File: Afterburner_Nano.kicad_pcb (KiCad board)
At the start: 4 copper layers, 37.9 x 36.5 mm, 86 parts, among them IC1 TPS25730DREFR, IC2 TVS3301DRBR, IC3 MCP1416T-E_OT, IC4 ADS1220IRVAR, IC5 MAX31865ATP+T, IC6 TVS3301DRBR, IC7 INA260AIPWR, IC8 AP7361E-33FGE-7, J1 USB4730-GF-A-KIT, J2 NTMFS5C612NLT1G, J3 Conn_01x04_Pin, J4 Conn_01x02_Pin, J5 USB4730-GF-A-KIT, J6 Conn_01x04_Pin, U1 TPS62933DRLR, U4 ESP32-C6-MINI-1

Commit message: layout changes
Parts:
- removed C6, C7: 330pF, Capacitor_SMD:C_0201_0603Metric
- added R29: 22, Resistor_SMD:R_0201_0603Metric, F.Cu at (197.3, 41.5)
- added R30: 22, Resistor_SMD:R_0201_0603Metric, F.Cu at (197.3, 40.7)
- added R31: 3k3, Resistor_SMD:R_0201_0603Metric, F.Cu at (188.1, 41.6)
- C14, C15: footprint Capacitor_SMD:C_0402_1005Metric -> Capacitor_SMD:C_0805_2012Metric
- C18: footprint Capacitor_SMD:C_0201_0603Metric -> Capacitor_SMD:C_0805_2012Metric
- moved C15 6.41 mm to (188.2, 31.1), turned to -90 degrees
- moved C18 5.27 mm to (190.3, 31.1), turned to -90 degrees
- moved C19 4.16 mm to (190.5, 24.6), turned to 0 degrees
- moved C16 3.99 mm to (178.4, 43.8), turned to -90 degrees
- moved C17 3.90 mm to (177.7, 43.8), turned to -90 degrees
- moved C14 2.46 mm to (190.3, 27.6)
- moved IC3 1.09 mm to (190.0, 21.8)
- moved R10 0.69 mm to (189.7, 19.1), turned to 0 degrees
- moved H4 0.62 mm to (204.7, 36.3)
- moved C21 0.54 mm to (191.4, 35.7)
- moved J2 0.42 mm to (183.2, 21.3)
- moved R4 0.13 mm to (200.0, 30.2)
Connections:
- C19 pad 1: +3v3 -> +5V
- IC3 pad 3: /Heater/HEATER_PWM -> /HEATER_PWM
- U4 pad 17: /D- -> /ESP-D-
- U4 pad 18: /D+ -> /ESP-D+
- U4 pad 19: /ALERT_INT -> unconnected-(U4-IO14-Pad19)
- U4 pad 20: /SDA -> /ALERT_INT
- U4 pad 22: /SCL -> /GPIO8
- U4 pad 24: /TEMP_CS -> /SDA
- U4 pad 25: /SCK -> /SCL
- U4 pad 26: /MOSI -> /TEMP_CS
- U4 pad 27: /MISO -> /SCK
- U4 pad 28: /LOADCELL_CS -> /MOSI
- U4 pad 29: /LOADCELL_DRDY -> /MISO
- U4 pad 30: unconnected-(U4-RXD0-Pad30) -> /LOADCELL_CS
- U4 pad 31: unconnected-(U4-TXD0-Pad31) -> /LOADCELL_DRDY
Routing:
- net +3V3: track 48.9 -> 92.1 mm, vias 4 -> 8
- net GND: track 16.7 -> 45.1 mm, vias 33 -> 68
- net /Heater/HEATER_PWM: track 16.3 -> 0.00 mm, vias 1 -> 0
- net /HEATER_PWM: track 15.7 -> 26.7 mm, vias 1 -> 2
- net /USB C PD Sink & Power/Reserved_36: track 0.06 -> 10.3 mm, vias 0 -> 2
- net /Heater/OUT_MOS: track 8.88 -> 0.14 mm
- net /ESP-D+: track 0.00 -> 6.35 mm
- net /ESP-D-: track 0.00 -> 5.59 mm
- net /D+: track 22.5 -> 17.7 mm
- net VCC: track 10.7 -> 6.41 mm, vias 8 -> 0
- net /SDA: track 38.8 -> 34.6 mm, vias 3 -> 2
- net /D-: track 21.7 -> 17.5 mm
- net /SCK: track 15.7 -> 12.0 mm
- net /USB C PD Sink & Power/LDO_3V3: track 20.2 -> 17.7 mm, vias 5 -> 4
- net /USB C PD Sink & Power/CC1: track 12.7 -> 10.2 mm, vias 3 -> 2
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- added copper zone on F.Cu, net +3V3
- added copper zone on In2.Cu, net +3V3
- added copper zone on In2.Cu, net /USB C PD Sink & Power/VBUS
- added copper zone on B.Cu, net GND
- added copper zone on In1.Cu, net GND
- added copper zone on In2.Cu, net GND
- removed copper zone on In2.Cu, net VCC
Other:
- board text removed: "Celestine S. Machuca 2025"
- board text removed: "M2"

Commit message: layout changes
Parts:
- added C22: 220p, Capacitor_SMD:C_0402_1005Metric, F.Cu at (202.9, 27.5)
- added C23: 220p, Capacitor_SMD:C_0402_1005Metric, F.Cu at (201.4, 27.0)
- added C6: 10u, Capacitor_SMD:C_0402_1005Metric, F.Cu at (200.8, 23.2)
- added IC9: LM66200DRLR, Footprints:SOTFL50P160X60-8N, F.Cu at (188.5, 35.6)
- added R32: 1k, Resistor_SMD:R_0201_0603Metric, F.Cu at (189.0, 34.0)
- added R33: 10k, Resistor_SMD:R_0201_0603Metric, F.Cu at (188.5, 37.3)
- R11: value 198.2k -> 100k
- R20: value 198.2k -> 11k
- R21: value 9.4k -> 0
- R22: value 198.2k -> 10M
- R23: value 162k -> 100k
- R25, R27: value 198.2k -> 18k
- R26: value 190k -> 100k
- moved C20 6.75 mm to (191.3, 34.9), turned to 180 degrees
- moved R14 6.14 mm to (182.7, 30.7)
- moved R24 6.14 mm to (184.7, 30.7)
- moved R13 6.14 mm to (183.7, 30.7)
- moved Css1 4.44 mm to (202.1, 33.4), turned to 0 degrees
- moved C10 2.97 mm to (192.5, 28.2), turned to 90 degrees
- moved C3 2.87 mm to (196.5, 37.6), turned to -90 degrees
- moved R4 2.48 mm to (202.1, 31.5), turned to 0 degrees
- moved L1 2.31 mm to (200.2, 37.8)
- moved Cboot1 2.30 mm to (201.6, 34.9)
- moved R28 2.15 mm to (199.6, 31.8), turned to 0 degrees
- moved C21 2.12 mm to (190.5, 37.6)
- moved IC6 2.11 mm to (206.1, 32.2)
- moved Cin1 1.89 mm to (196.9, 32.6)
- moved Cinx1 1.89 mm to (197.1, 34.4)
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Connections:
- net /CONNECTOR/VBUS renamed /VBUS_COM_CONNECTOR
- C20 pad 1: +5V -> /+5V_LDO
- IC1 pad 38: /USB C PD Sink & Power/VIN_3V3 -> +3V3
- IC8 pad 5: +5V -> /+5V_LDO
- IC8 pad 8: +5V -> /+5V_LDO
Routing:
- net +3V3: track 92.1 -> 65.5 mm, vias 8 -> 9
- net /VBUS_COM_CONNECTOR: track 0.00 -> 22.3 mm, vias 0 -> 3
- net GND: track 45.1 -> 31.6 mm, vias 68 -> 59
- net /+5V_LDO: track 0.00 -> 9.29 mm
- net +5V: track 33.7 -> 41.9 mm
- net Net-(U1-SS): track 2.63 -> 0.00 mm
- net /USB C PD Sink & Power/VIN_3V3: track 1.66 -> 0.00 mm, vias 1 -> 0
- net /USB C PD Sink & Power/CC1: track 10.2 -> 11.7 mm
- net /USB C PD Sink & Power/CC2: track 7.55 -> 8.89 mm
- net /USB C PD Sink & Power/Reserved_36: track 10.3 -> 11.5 mm
- net Net-(U1-RT): track 1.15 -> 0.00 mm
- net Net-(IC9-ST): track 0.00 -> 1.13 mm
- net /HEATER_PWM: track 26.7 -> 27.7 mm
- net Net-(IC9-~{ON}): track 0.00 -> 0.91 mm
- net /PD_INT: track 26.7 -> 26.1 mm
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- added copper zone on F.Cu, net Net-(U1-RT)
- added copper zone on F.Cu, net Net-(U1-SS)

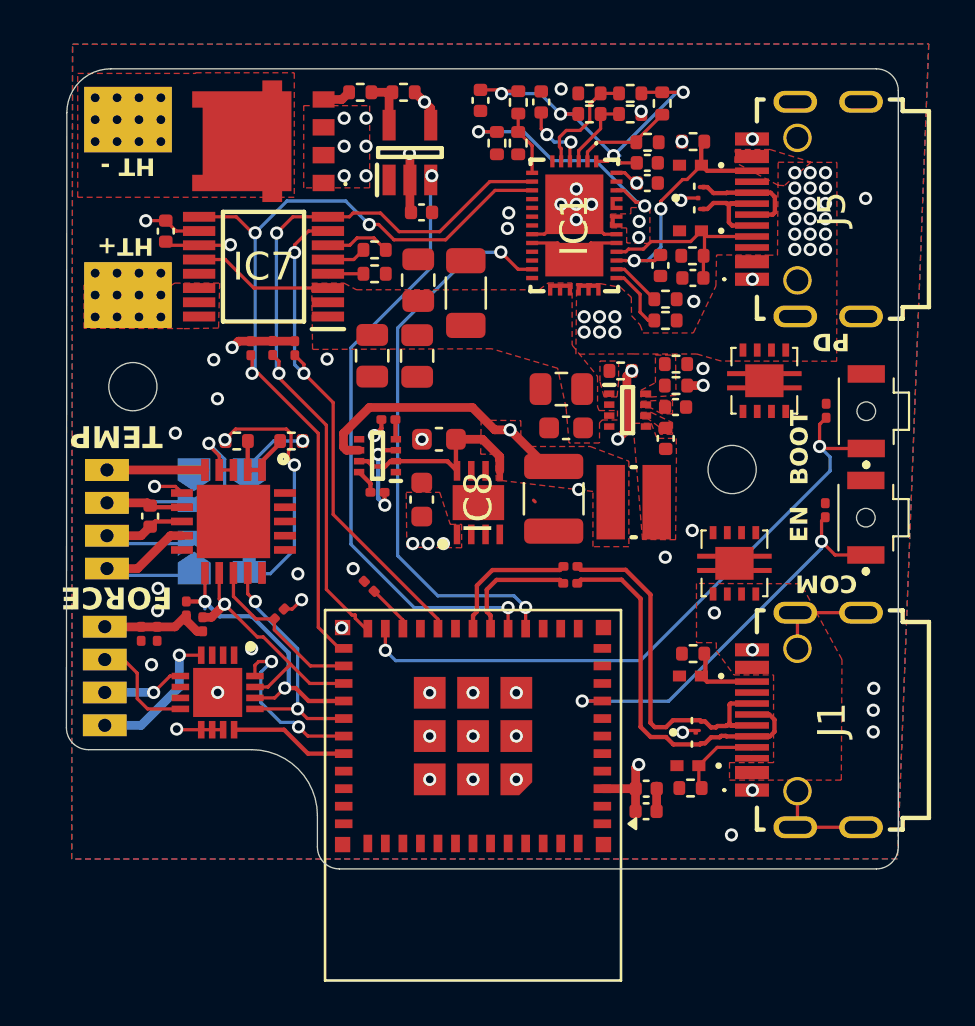
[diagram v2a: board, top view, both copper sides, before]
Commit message: Power layout changes
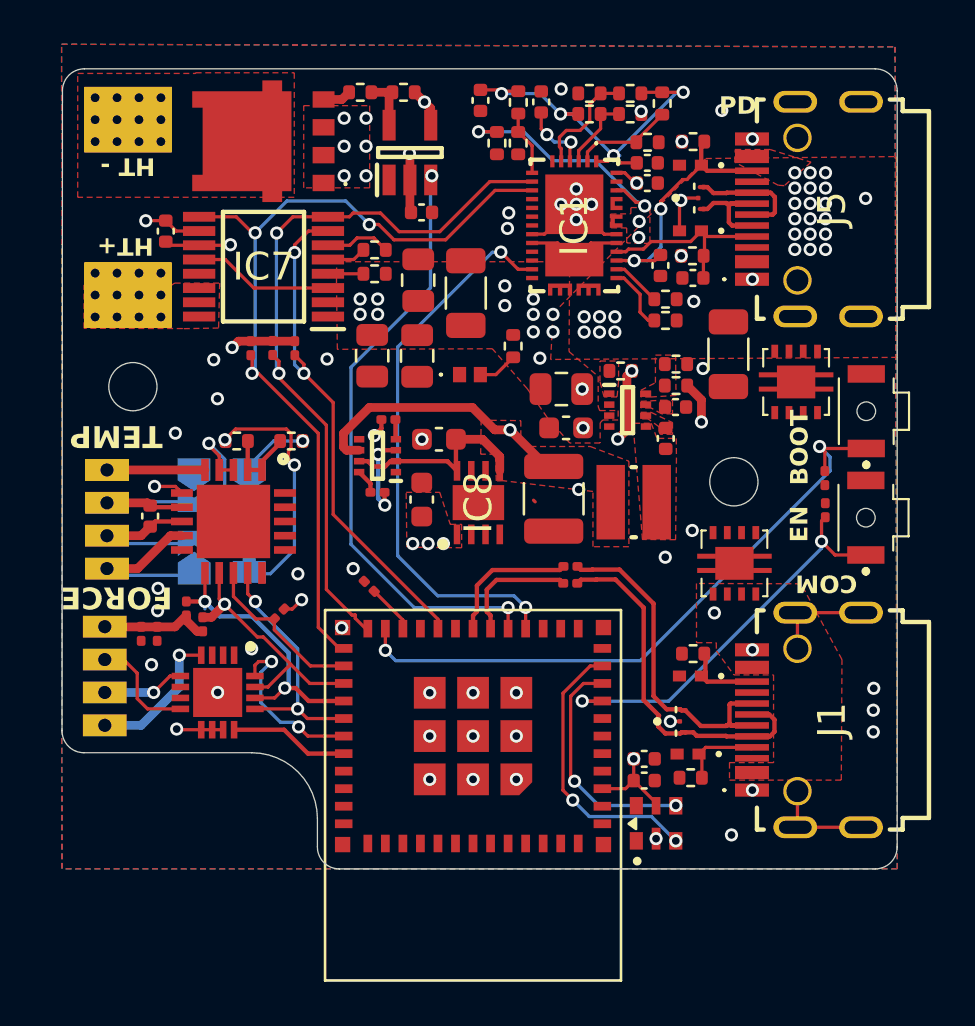
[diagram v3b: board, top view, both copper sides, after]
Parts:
- added C7: 4.7u, Capacitor_SMD:C_1206_3216Metric, F.Cu at (204.5, 31.0)
- added D7: BB-2020BGR-TRB, Footprints:LED_BB-2020BGR-TRB, F.Cu at (201.2, 52.4)
- added LED1: VLMTG1500-GS08, Footprints:VLMTG1500GS08, F.Cu at (192.7, 31.9)
- added R34: 10k, Resistor_SMD:R_0402_1005Metric, F.Cu at (194.7, 30.6)
- moved C1 3.07 mm to (208.9, 36.7), turned to 90 degrees
- moved C5 2.39 mm to (200.7, 49.5)
- moved IC6 1.45 mm to (207.6, 32.3)
- moved D1 0.88 mm to (202.4, 47.8)
- moved H4 0.57 mm to (204.8, 36.8)
- moved D3 0.53 mm to (202.7, 49.3)
- moved R6 0.47 mm to (202.8, 50.3)
- moved C4 0.38 mm to (200.7, 50.5)
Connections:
- U4 pad 10: unconnected-(U4-IO5-Pad10) -> /LED_DIN
- U4 pad 9: unconnected-(U4-IO4-Pad9) -> /LED_CLK
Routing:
- net +3V3: track 65.5 -> 20.2 mm
- net /LED_DIN: track 0.00 -> 12.8 mm, vias 0 -> 2
- net /LED_CLK: track 0.00 -> 10.7 mm, vias 0 -> 2
- net +5V: track 41.9 -> 49.3 mm
- net Net-(LED1-A): track 0.00 -> 1.82 mm
- net /D+: track 17.7 -> 16.4 mm
- net /D-: track 17.5 -> 16.7 mm
- net /PD_INT: track 26.1 -> 25.6 mm
- net GND: track 31.6 -> 31.7 mm, vias 59 -> 62
- net VCC: vias 0 -> 14
- added copper zone on In2.Cu, net VCC
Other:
- board size 37.9 x 36.5 mm -> 38.1 x 36.5 mm

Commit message: Layout Changes, MPN Added
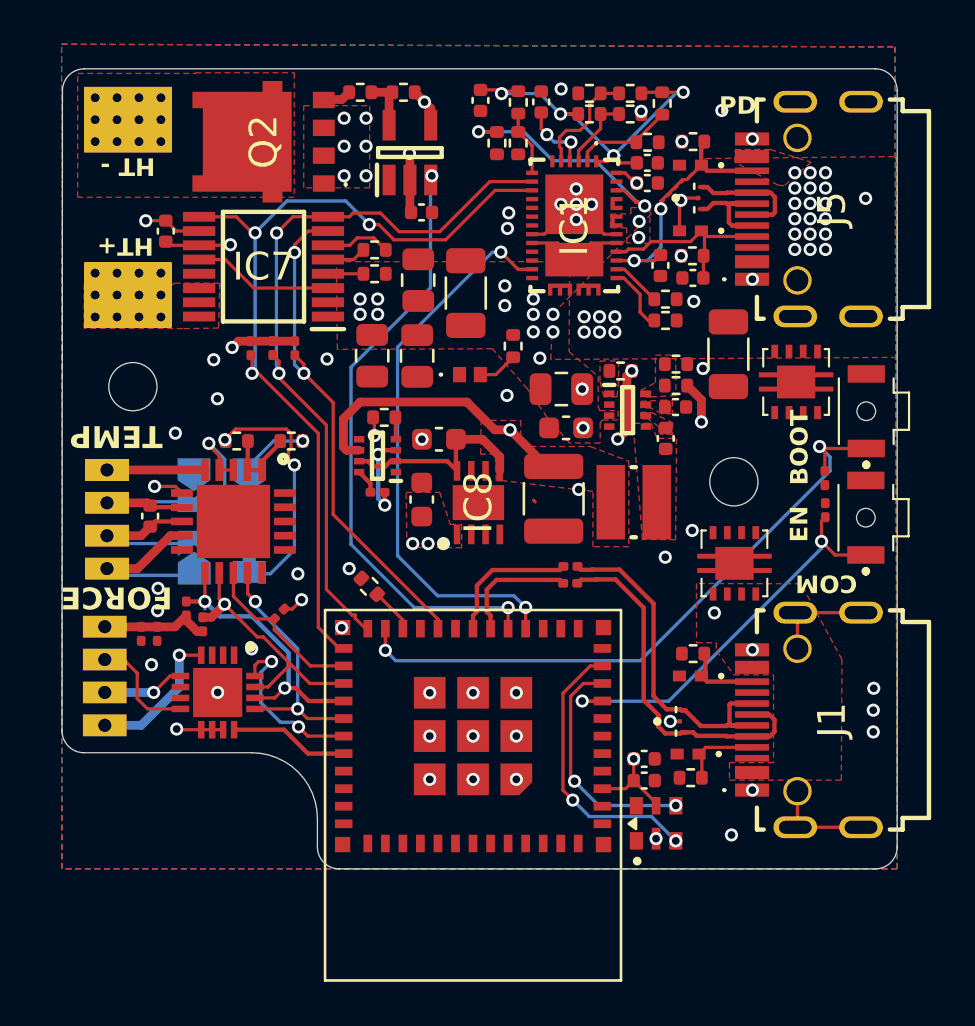
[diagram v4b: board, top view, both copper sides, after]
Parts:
- removed J2: NTMFS5C612NLT1G, Footprints:NTMFS5C612NLT1G
- added Q2: NTMFS5C612NLT1G, Footprints:NTMFS5C612NLT1G, F.Cu at (183.2, 21.3)
- R28: value 9.09k -> 9.1k
- R31, R32: footprint Resistor_SMD:R_0201_0603Metric -> Resistor_SMD:R_0402_1005Metric
- moved R32 0.21 mm to (188.8, 33.9)
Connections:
- net /Heater/IN- renamed /Heater/IN+
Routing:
- net +5V: track 49.3 -> 49.9 mm
- net GND: vias 62 -> 63

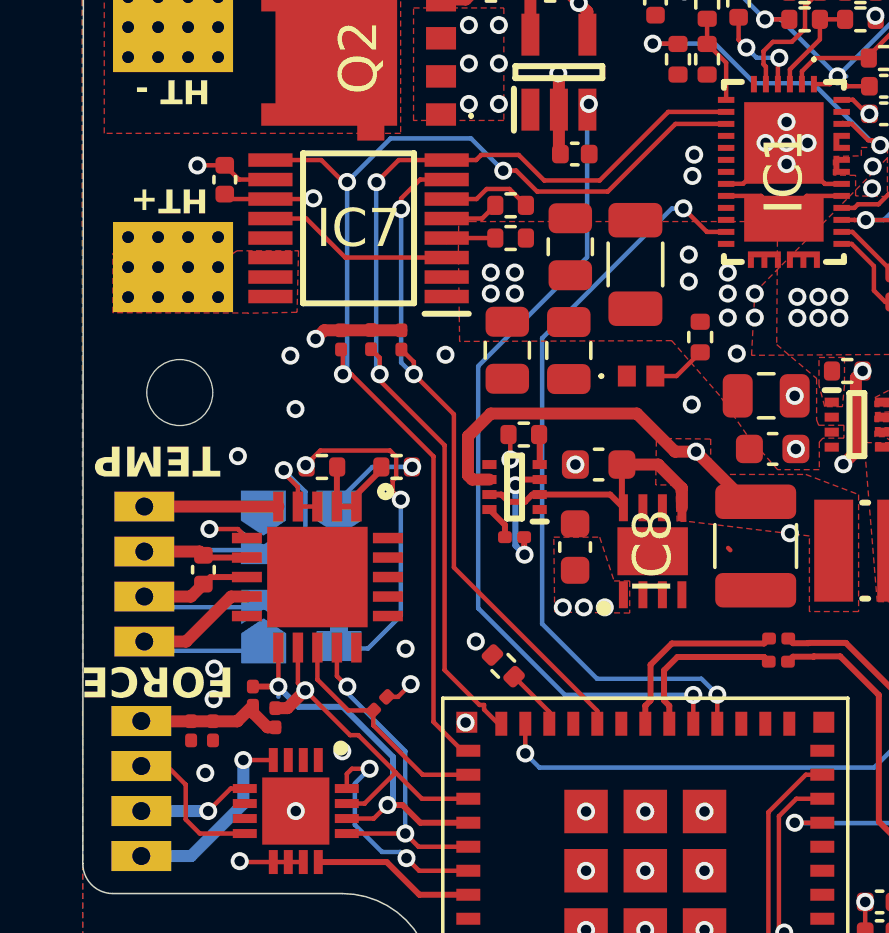
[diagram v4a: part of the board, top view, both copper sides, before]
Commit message: change res to correct size
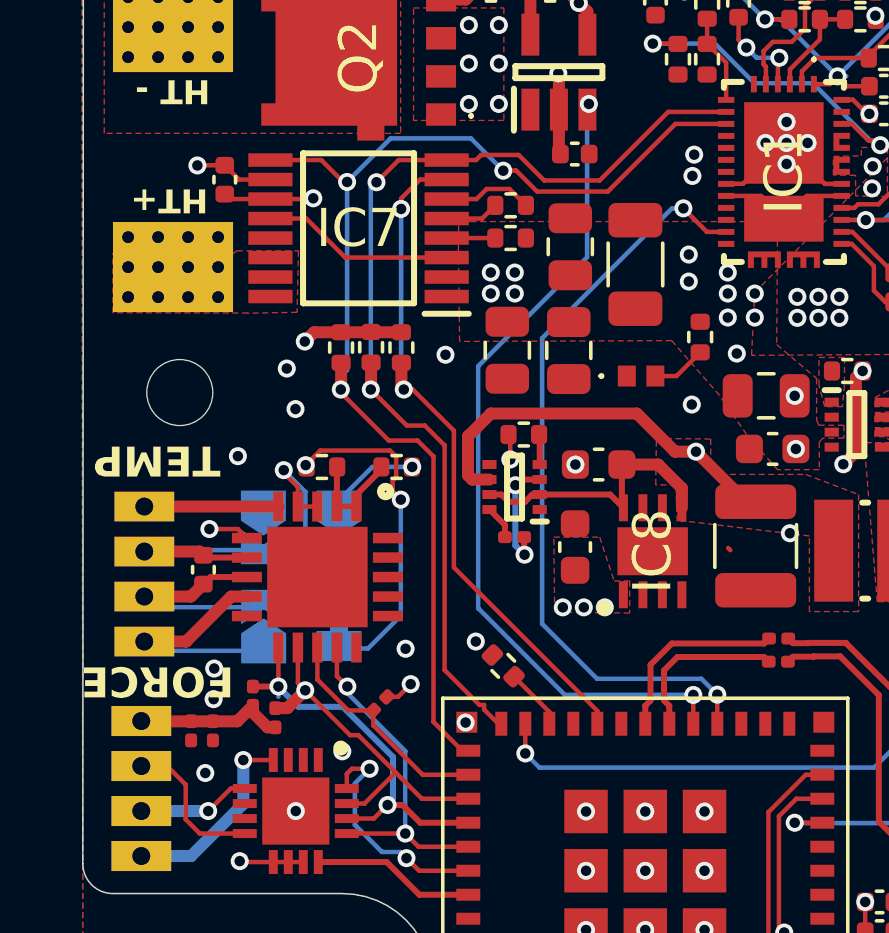
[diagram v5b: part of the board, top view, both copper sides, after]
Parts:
- R13, R14, R24: footprint Resistor_SMD:R_0201_0603Metric -> Resistor_SMD:R_0402_1005Metric
- moved R13 0.25 mm to (183.7, 31.0)
- moved R14 0.25 mm to (182.7, 31.0)
- moved R24 0.25 mm to (184.7, 31.0)
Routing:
- net /SCL: track 39.6 -> 40.1 mm
